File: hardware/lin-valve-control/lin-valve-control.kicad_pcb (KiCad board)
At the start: 4 copper layers, 78.2 x 43.2 mm, 42 parts, among them J1 Screw_Terminal_01x04, J2 Screw_Terminal_01x02, J3 QWIIC Connector, J4 Screw_Terminal_01x03, J5 Screw_Terminal_01x03, J6 DIN5, J7 DIN5, Q1 2N7002, Q2 2N7002, Q3 2N7002, Q4 2N7002, Q5 SUD50P04-08, Q6 SUD50P04-08, U1 Arduino_Nano_v3.x, U2 DRV8833PWP, U3 TJA1021T

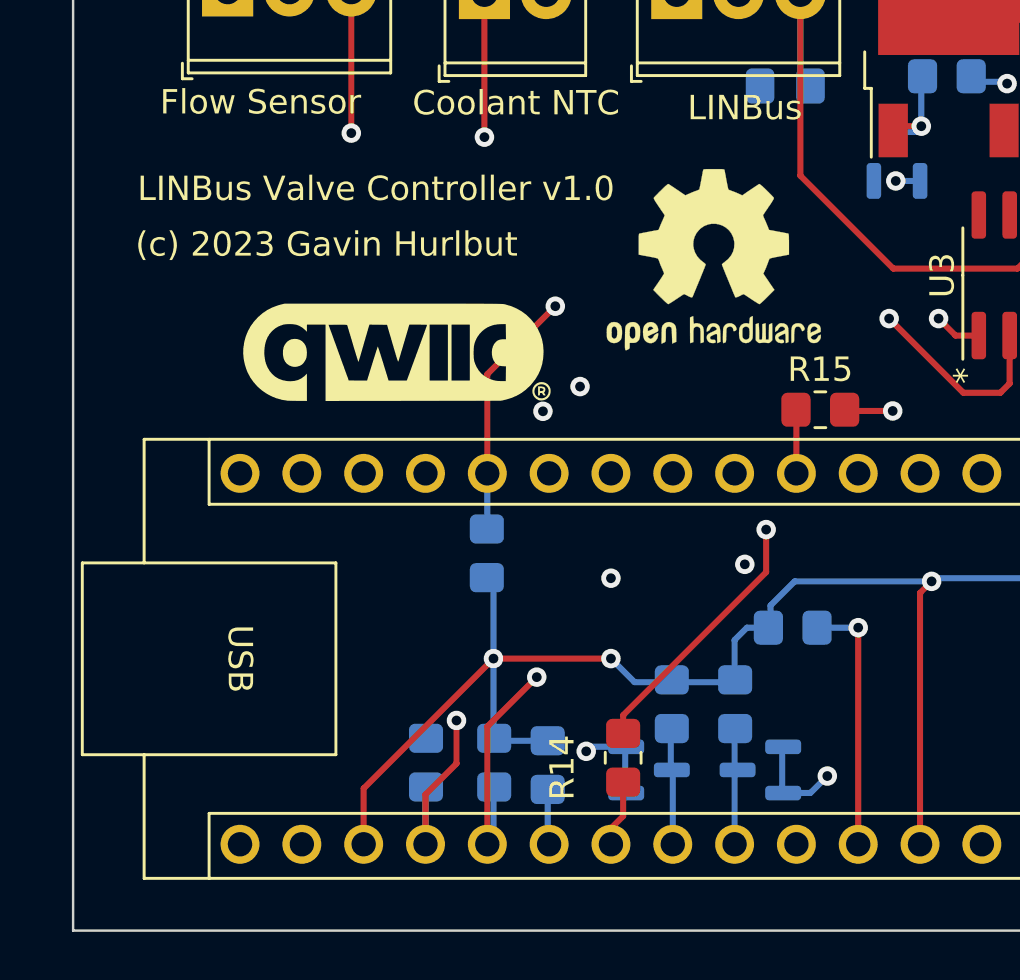
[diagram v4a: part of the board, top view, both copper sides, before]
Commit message: Add a connector to attach 20x4 LCD on an I2C backpack
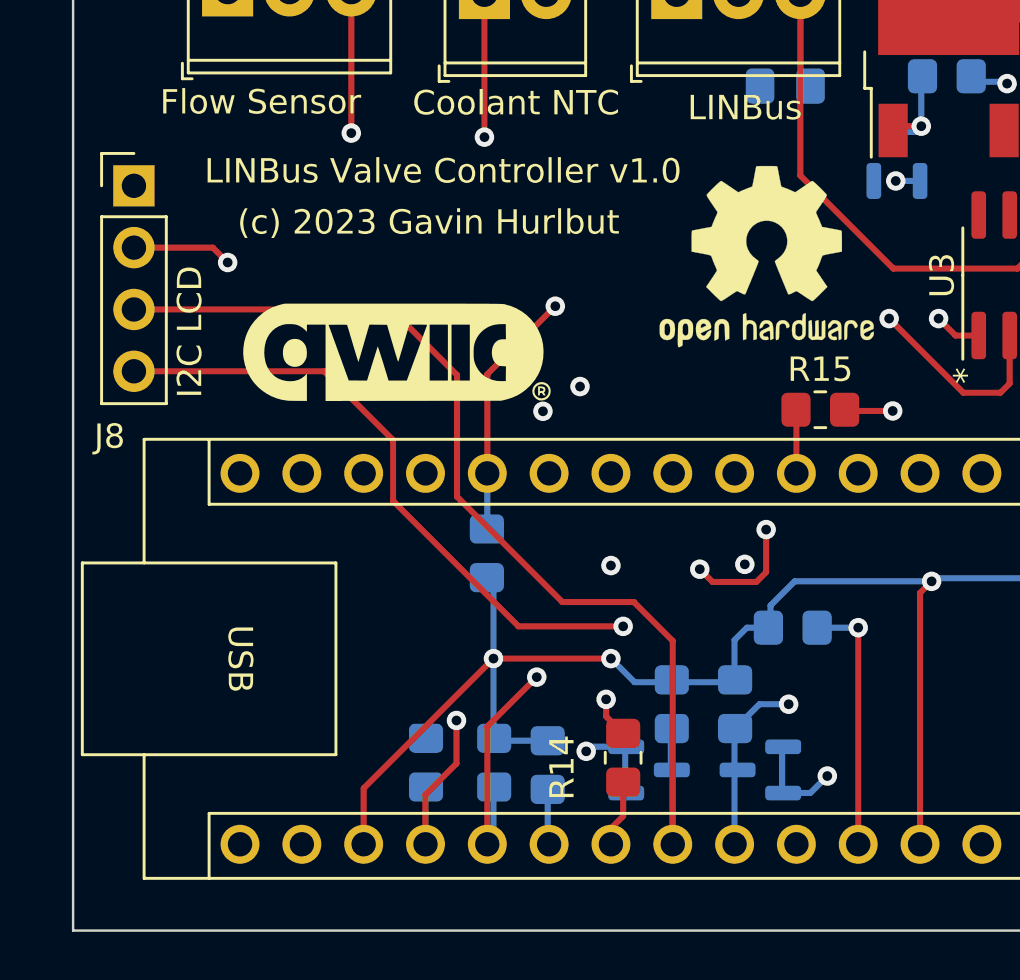
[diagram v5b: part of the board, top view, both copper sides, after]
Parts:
- added J8: I2C LCD, Connector_PinHeader_2.54mm:PinHeader_1x04_P2.54mm_Vertical, F.Cu at (154.9, 71.0)
- moved REF** 2.18 mm to (180.9, 73.9)
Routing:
- net SDA5V: track 4.90 -> 44.0 mm
- net SCL5V: track 4.90 -> 41.5 mm, vias 0 -> 2
- net +5V: track 90.8 -> 95.0 mm, vias 3 -> 4
- net Net-(Q3-Pad1): track 28.3 -> 31.0 mm, vias 2 -> 4
- net VALVE1_CLOSED: track 48.5 -> 50.1 mm
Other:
- board text added: "I2C LCD"

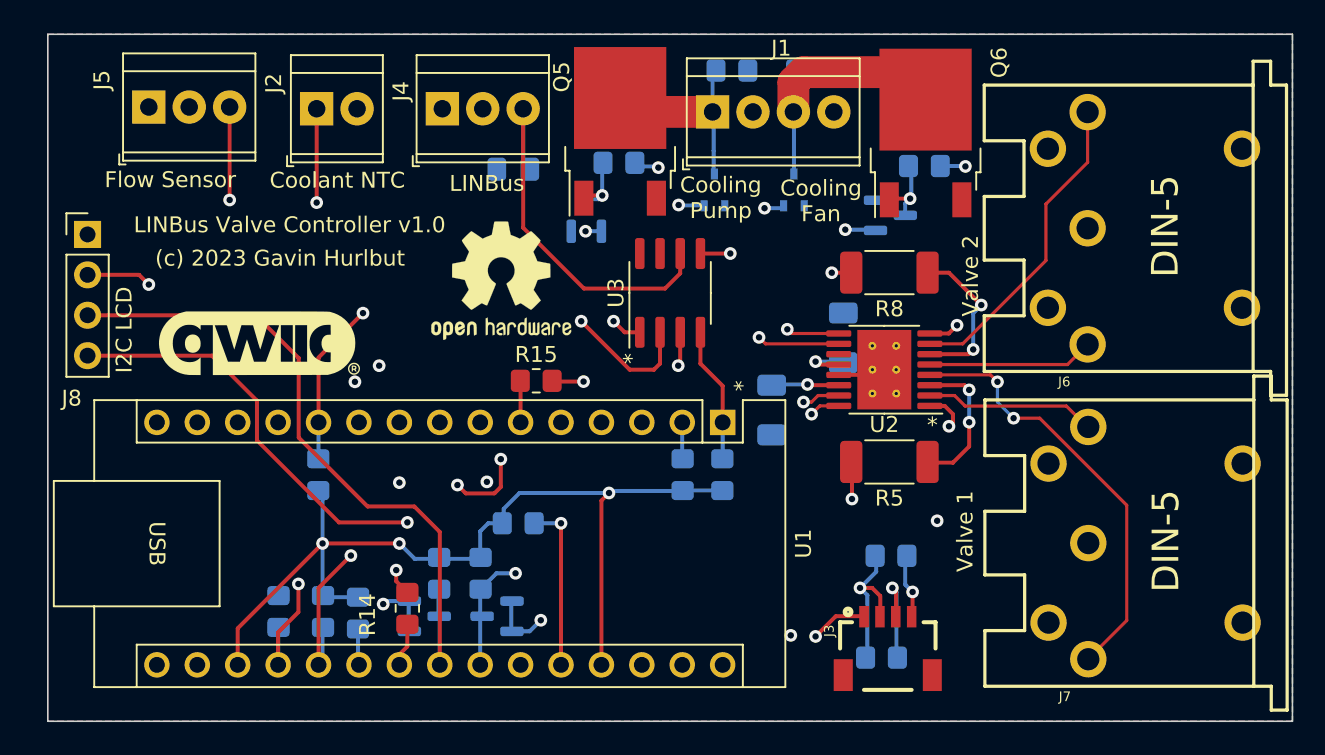
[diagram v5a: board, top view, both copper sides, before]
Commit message: Completely redo the valve controller.  One valve only.
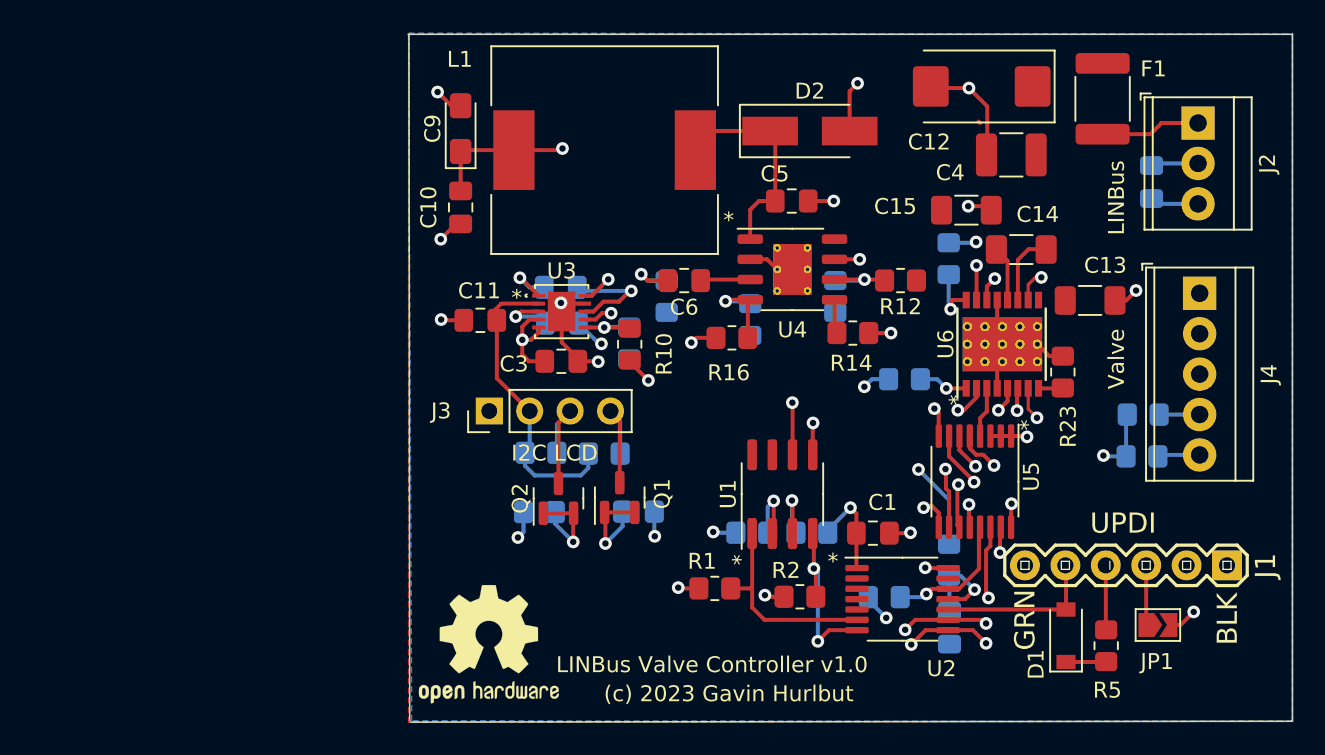
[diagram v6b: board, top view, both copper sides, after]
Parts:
- removed G***: LOGO, Beirdo:qwiic-logo
- removed J5: Screw_Terminal_01x03, TerminalBlock_TE-Connectivity:TerminalBlock_TE_282834-3_1x03_P2.54mm_Horizontal
- removed J6, J7: DIN5, SparkFun-Connectors:DIN5-RA-PTH
- removed J8: I2C LCD, Connector_PinHeader_2.54mm:PinHeader_1x04_P2.54mm_Vertical
- removed Q3, Q4: 2N7002, Package_TO_SOT_SMD:SOT-23
- removed Q5, Q6: SUD50P04-08, Package_TO_SOT_SMD:TO-252-2
- added C10: 10uF, Capacitor_SMD:C_0805_2012Metric_Pad1.18x1.45mm_HandSolder, F.Cu at (178.3, 69.3)
- added C11: 10uF, Capacitor_SMD:C_0805_2012Metric_Pad1.18x1.45mm_HandSolder, F.Cu at (179.6, 76.4)
- added C12: 100uF Ta 25V, Capacitor_Tantalum_SMD:CP_EIA-7343-20_Kemet-V_Pad2.25x2.55mm_HandSolder, F.Cu at (211.1, 61.7)
- added C13: 100nF 25V, Capacitor_SMD:C_1206_3216Metric_Pad1.33x1.80mm_HandSolder, F.Cu at (217.9, 75.2)
- added C14: 100nF 25V, Capacitor_SMD:C_1206_3216Metric_Pad1.33x1.80mm_HandSolder, F.Cu at (213.6, 72.0)
- added C15: 100nF 25V, Capacitor_SMD:C_1206_3216Metric_Pad1.33x1.80mm_HandSolder, F.Cu at (210.1, 69.5)
- added C16: 1nF, Capacitor_SMD:C_0805_2012Metric_Pad1.18x1.45mm_HandSolder, B.Cu at (209.1, 95.7)
- added C4: 10uF 100V, Capacitor_SMD:C_1210_3225Metric_Pad1.33x2.70mm_HandSolder, F.Cu at (213.0, 66.0)
- added C5: 100nF, Capacitor_SMD:C_0805_2012Metric_Pad1.18x1.45mm_HandSolder, F.Cu at (199.2, 68.9)
- added C6: 10nF, Capacitor_SMD:C_0805_2012Metric_Pad1.18x1.45mm_HandSolder, F.Cu at (192.4, 73.9)
- added C7: 2.2uF, Capacitor_SMD:C_0805_2012Metric_Pad1.18x1.45mm_HandSolder, B.Cu at (184.7, 76.6)
- added C8: 2.2uF, Capacitor_SMD:C_0805_2012Metric_Pad1.18x1.45mm_HandSolder, B.Cu at (184.6, 74.3)
- added C9: 100uF Ta 6V, Capacitor_Tantalum_SMD:CP_EIA-3216-10_Kemet-I_Pad1.58x1.35mm_HandSolder, F.Cu at (178.3, 64.3)
- added F1: 3A Polyfuse, Resistor_SMD:R_1812_4532Metric_Pad1.30x3.40mm_HandSolder, F.Cu at (218.7, 62.5)
- added JP1: Solder Jumper, Jumper:SolderJumper-2_P1.3mm_Open_TrianglePad1.0x1.5mm, F.Cu at (222.2, 95.5)
- added L1: 33uH 5A 88mOhm, Beirdo:PM4346.333NLT, F.Cu at (187.4, 65.7)
- added R20: 10k, Resistor_SMD:R_0805_2012Metric_Pad1.20x1.40mm_HandSolder, B.Cu at (221.2, 82.3)
- added R21: 10k, Resistor_SMD:R_0805_2012Metric_Pad1.20x1.40mm_HandSolder, B.Cu at (221.2, 85.0)
- added R22: 10k, Resistor_SMD:R_0805_2012Metric_Pad1.20x1.40mm_HandSolder, B.Cu at (209.1, 91.5)
- added R23: 200m, Resistor_SMD:R_0805_2012Metric_Pad1.20x1.40mm_HandSolder, F.Cu at (216.2, 79.7)
- added R24: 10k, Resistor_SMD:R_0805_2012Metric_Pad1.20x1.40mm_HandSolder, B.Cu at (206.2, 80.1)
- added U4: BD9G341EFJ, Package_SO:HTSOP-8-1EP_3.9x4.9mm_P1.27mm_EP2.4x3.2mm_ThermalVias, F.Cu at (199.2, 73.2)
- added U5: TCA9534, Package_SO:TSSOP-16_4.4x5mm_P0.65mm, F.Cu at (210.7, 86.5)
- added U6: DRV8801PWP, Package_SO:HTSSOP-16-1EP_4.4x5mm_P0.65mm_EP3.4x5mm_Mask3x3mm_ThermalVias, F.Cu at (212.4, 77.9)
- C1: value 10uF 16V -> 100nF; footprint Capacitor_SMD:C_1206_3216Metric_Pad1.33x1.80mm_HandSolder -> Capacitor_SMD:C_0805_2012Metric_Pad1.18x1.45mm_HandSolder; moved to F.Cu
- C3: value 2.2uF 6.3V -> 2.2uF; footprint Capacitor_SMD:C_1206_3216Metric_Pad1.33x1.80mm_HandSolder -> Capacitor_SMD:C_0805_2012Metric_Pad1.18x1.45mm_HandSolder; moved to F.Cu
- D1: value BAT54SW -> BAT42W-V; footprint Package_TO_SOT_SMD:SOT-323_SC-70 -> Diode_SMD:D_SOD-123; moved to F.Cu
- D2: value BAT54SW -> BYS10-35; footprint Package_TO_SOT_SMD:SOT-323_SC-70 -> Diode_SMD:D_SMA_Handsoldering; moved to F.Cu
- J1: value Screw_Terminal_01x04 -> UPDI; footprint TerminalBlock_TE-Connectivity:TerminalBlock_TE_282834-4_1x04_P2.54mm_Horizontal -> Beirdo:FTDI_BASIC
- J2: value Screw_Terminal_01x02 -> Screw_Terminal_01x03; footprint TerminalBlock_TE-Connectivity:TerminalBlock_TE_282834-2_1x02_P2.54mm_Horizontal -> TerminalBlock_TE-Connectivity:TerminalBlock_TE_282834-3_1x03_P2.54mm_Horizontal
- J3: value QWIIC Connector -> I2C LCD; footprint SparkFun-Connectors:1X04_1MM_RA -> Connector_PinHeader_2.54mm:PinHeader_1x04_P2.54mm_Vertical
- J4: value Screw_Terminal_01x03 -> Screw_Terminal_01x05; footprint TerminalBlock_TE-Connectivity:TerminalBlock_TE_282834-3_1x03_P2.54mm_Horizontal -> TerminalBlock_TE-Connectivity:TerminalBlock_TE_282834-5_1x05_P2.54mm_Horizontal
- Q1, Q2, R1, R2: moved to F.Cu
- R10: value 10k -> 357k 1%; moved to F.Cu
- R11: value 10k -> 100k 1%
- R12: value 10k -> 909k 1%; moved to F.Cu
- R13: value 10k -> 324k 1%
- R14: value 10R -> 47k
- R15: value 10R -> 6k2; moved to B.Cu
- R16: value 10k -> 1k3; moved to F.Cu
- R17: value 10k -> 560R
- R18: value 10R -> 100k
- R19: value 10R -> 10k
- R5: value 2R 2W -> 470R; footprint Resistor_SMD:R_2010_5025Metric_Pad1.40x2.65mm_HandSolder -> Resistor_SMD:R_0805_2012Metric_Pad1.20x1.40mm_HandSolder
- R8: value 2R 2W -> 10k; footprint Resistor_SMD:R_2010_5025Metric_Pad1.40x2.65mm_HandSolder -> Resistor_SMD:R_0805_2012Metric_Pad1.20x1.40mm_HandSolder; moved to B.Cu
- U1: value Arduino_Nano_v3.x -> TJA1021T; footprint Module:Arduino_Nano -> Package_SO:SOIC-8_3.9x4.9mm_P1.27mm
- U2: value DRV8833PWP -> ATtiny424-X; footprint Package_SO:HTSSOP-16-1EP_4.4x5mm_P0.65mm_EP3.4x5mm_Mask2.46x2.31mm_ThermalVias -> Package_SO:TSSOP-14_4.4x5mm_P0.65mm
- U3: value TJA1021T -> LTC3203BEDD-PBF; footprint Package_SO:SOIC-8_3.9x4.9mm_P1.27mm -> UltraLibrarian:LTC3203BEDD-PBF
- moved J2 55.4 mm to (224.7, 64.0), turned to -90 degrees
- moved J4 49.0 mm to (224.8, 74.7), turned to -90 degrees
- moved J1 43.1 mm to (226.5, 91.8), turned to 180 degrees
- moved C2 40.1 mm to (221.8, 67.7), turned to 90 degrees
- moved R12 40.0 mm to (206.0, 73.9), turned to 180 degrees
- moved D1 35.7 mm to (216.4, 96.2)
- moved R19 33.4 mm to (205.0, 93.8)
- moved R14 32.9 mm to (203.0, 77.2), turned to 0 degrees
- moved R3 30.2 mm to (196.7, 89.8), turned to 0 degrees
- moved J3 28.2 mm to (180.2, 82.1), turned to 90 degrees
- moved R8 26.7 mm to (183.3, 88.5), turned to 0 degrees
- moved R10 25.6 mm to (189.0, 77.9), turned to 90 degrees
- moved R11 25.3 mm to (188.9, 77.8), turned to 90 degrees
- moved R4 23.6 mm to (200.4, 89.8), turned to 180 degrees
- moved REF** 22.9 mm to (180.1, 96.8)
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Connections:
- C1 pad 1: +12V -> GND
- C1 pad 2: GND -> +3V3
- C3 pad 1: Net-(C3-Pad1) -> +3V3
- D1 pad 1: GND -> Net-(D1-Pad1)
- D1 pad 2: +12V -> UPDI
- D2 pad 1: GND -> Net-(C5-Pad2)
- D2 pad 2: +12V -> GND
- J1 pad 1: COOLANT_PUMP -> GND
- J1 pad 2: GND -> unconnected-(J1-Pad2)
- J1 pad 3: COOLING_FAN -> Net-(J1-Pad3)
- J1 pad 4: GND -> Net-(J1-Pad4)
- J2 pad 1: COOLANT_NTC -> +BATT
- J3 pad 2: +3V3 -> +5V
- J3 pad 3: SDA3V -> SDA5V
- J3 pad 4: SCL3V -> SCL5V
- J4 pad 1: +12V -> VALVE+
- J4 pad 2: GND -> VALVE-
- J4 pad 3: LIN -> GND
- R1 pad 1: +5V -> +3V3
- R1 pad 2: COOLANT_NTC -> RXD
- R10 pad 1: +5V -> +3V3
- R10 pad 2: ~{LIN_WAKE} -> Net-(R10-Pad2)
- R11 pad 1: +3V3 -> GND
- R11 pad 2: SDA3V -> Net-(R10-Pad2)
- R12 pad 1: +5V -> +12V
- R12 pad 2: ~{MOTOR_FAULT} -> Net-(R12-Pad2)
- R13 pad 1: +3V3 -> Net-(R12-Pad2)
- R13 pad 2: SCL3V -> GND
- R14 pad 1: PUMP_EN -> Net-(R14-Pad1)
- R14 pad 2: Net-(Q3-Pad1) -> GND
- R15 pad 1: FAN_PWM -> Net-(C6-Pad2)
- R15 pad 2: Net-(Q4-Pad1) -> GND
- R16 pad 1: +12V -> +3V3
- R16 pad 2: Net-(Q3-Pad3) -> Net-(R16-Pad2)
- R17 pad 1: +12V -> Net-(R16-Pad2)
- R17 pad 2: Net-(Q4-Pad3) -> GND
- R18 pad 1: COOLANT_PUMP -> +3V3
- R18 pad 2: GND -> Net-(R18-Pad2)
- R19 pad 1: COOLING_FAN -> +3V3
- R19 pad 2: GND -> ~{I2C_INT}
- R2 pad 1: +5V -> +3V3
- R2 pad 2: RXD -> TXD
- R3 pad 1: MOTOR_EN -> +3V3
- R3 pad 2: GND -> ~{LIN_SLP}
- R4 pad 1: +5V -> +3V3
- R4 pad 2: SDA5V -> ~{LIN_WAKE}
- R5 pad 1: Net-(R5-Pad1) -> Net-(D1-Pad1)
- R5 pad 2: GND -> Net-(J1-Pad4)
- R6 pad 2: TXD -> SDA5V
- R8 pad 1: Net-(R8-Pad1) -> +3V3
- R8 pad 2: GND -> SDA3V
- R9 pad 1: +5V -> +3V3
- R9 pad 2: ~{LIN_SLP} -> SCL3V
- U1 pad 1: TXD -> RXD
- U1 pad 2: RXD -> ~{LIN_SLP}
- U1 pad 3: unconnected-(U1-Pad3) -> ~{LIN_WAKE}
- U1 pad 4: GND -> TXD
- U1 pad 5: FLOW_PULSE -> GND
- U1 pad 6: FAN_PWM -> LIN
- U1 pad 7: VALVE_IN1+ -> +12V
- U1 pad 8: VALVE_IN1- -> unconnected-(U1-Pad8)
- U2 pad 1: MOTOR_EN -> +3V3
- U2 pad 10: VALVE_IN2- -> UPDI
- U2 pad 11: unconnected-(U2-Pad11) -> VPROPI
- U2 pad 12: +12V -> ~{I2C_INT}
- U2 pad 13: GND -> ~{RESET}
- U2 pad 14: Net-(C3-Pad1) -> GND
- U2 pad 2: VALVE1+ -> unconnected-(U2-Pad2)
- U2 pad 3: Net-(R5-Pad1) -> unconnected-(U2-Pad3)
- U2 pad 4: VALVE1- -> unconnected-(U2-Pad4)
- U2 pad 5: VALVE2- -> unconnected-(U2-Pad5)
- U2 pad 6: Net-(R8-Pad1) -> RXD
- U2 pad 7: VALVE2+ -> TXD
- U2 pad 8: ~{MOTOR_FAULT} -> SDA3V
- U2 pad 9: VALVE_IN2+ -> SCL3V
- U3 pad 1: RXD -> Net-(C8-Pad1)
- U3 pad 2: ~{LIN_SLP} -> +5V
- U3 pad 3: ~{LIN_WAKE} -> Net-(C7-Pad2)
- U3 pad 4: TXD -> +3V3
- U3 pad 5: GND -> +3V3
- U3 pad 6: LIN -> Net-(R10-Pad2)
- U3 pad 7: +12V -> +3V3
- U3 pad 8: unconnected-(U3-Pad8) -> Net-(C8-Pad2)
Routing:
- net +5V: track 95.0 -> 18.9 mm, vias 4 -> 0
- net VALVE2_OPEN: track 63.1 -> 0.00 mm
- net ~{MOTOR_FAULT}: track 59.9 -> 0.00 mm, vias 3 -> 0
- net VALVE2_CLOSED: track 57.4 -> 0.00 mm
- net MOTOR_EN: track 56.0 -> 0.00 mm, vias 2 -> 0
- net VALVE1_CLOSED: track 50.1 -> 0.00 mm, vias 1 -> 0
- net VALVE1_OPEN: track 48.1 -> 0.00 mm
- net COOLANT_NTC: track 44.9 -> 0.00 mm, vias 2 -> 0
- net VALVE_IN2-: track 40.2 -> 0.00 mm, vias 1 -> 0
- net VALVE_IN2+: track 37.8 -> 0.00 mm, vias 1 -> 0
- net SDA5V: track 44.0 -> 7.82 mm
- net FLOW_PULSE: track 34.8 -> 0.00 mm, vias 2 -> 0
- net SCL5V: track 41.5 -> 7.67 mm, vias 2 -> 0
- net GND: track 11.6 -> 44.7 mm, vias 4 -> 14
- net Net-(Q3-Pad1): track 31.0 -> 0.00 mm, vias 4 -> 0
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- added copper zone on In2.Cu, net +3V3
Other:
- board size 78.2 x 43.2 mm -> 55.6 x 43.2 mm
- board text added: "Valve"
- board text removed: "Coolant NTC"
- board text removed: "Cooling Fan"
- board text removed: "Cooling Pump"
- board text removed: "Flow Sensor"
- board text removed: "Valve 1"
- board text removed: "Valve 2"

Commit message: Add PCA9536 for the LINBus Address
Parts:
- added JP2: A3, Jumper:SolderJumper-2_P1.3mm_Open_TrianglePad1.0x1.5mm, B.Cu at (194.1, 97.0)
- added JP3: A2, Jumper:SolderJumper-2_P1.3mm_Open_TrianglePad1.0x1.5mm, B.Cu at (191.4, 97.0)
- added JP4: A1, Jumper:SolderJumper-2_P1.3mm_Open_TrianglePad1.0x1.5mm, B.Cu at (188.8, 97.1)
- added JP5: A0, Jumper:SolderJumper-2_P1.3mm_Open_TrianglePad1.0x1.5mm, B.Cu at (186.3, 97.2)
- added U3: PCA9536DP, Package_SO:TSSOP-8_3x3mm_P0.65mm, F.Cu at (187.9, 93.2)
- renumbered J3 to J2, J2 to J3, U3 to U4, U4 to U5, U5 to U6, U6 to U7
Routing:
- net Net-(JP5-Pad2): track 0.00 -> 9.66 mm, vias 0 -> 2
- net Net-(JP4-Pad2): track 0.00 -> 8.13 mm, vias 0 -> 1
- net Net-(JP3-Pad2): track 0.00 -> 7.65 mm, vias 0 -> 1
- net Net-(JP2-Pad2): track 0.00 -> 5.65 mm, vias 0 -> 1
- net SDA3V: track 44.7 -> 47.7 mm, vias 4 -> 5
- net GND: track 44.7 -> 47.5 mm, vias 14 -> 15
- net SCL3V: track 39.7 -> 41.5 mm, vias 4 -> 5
- net +3V3: track 46.4 -> 47.7 mm, vias 17 -> 18

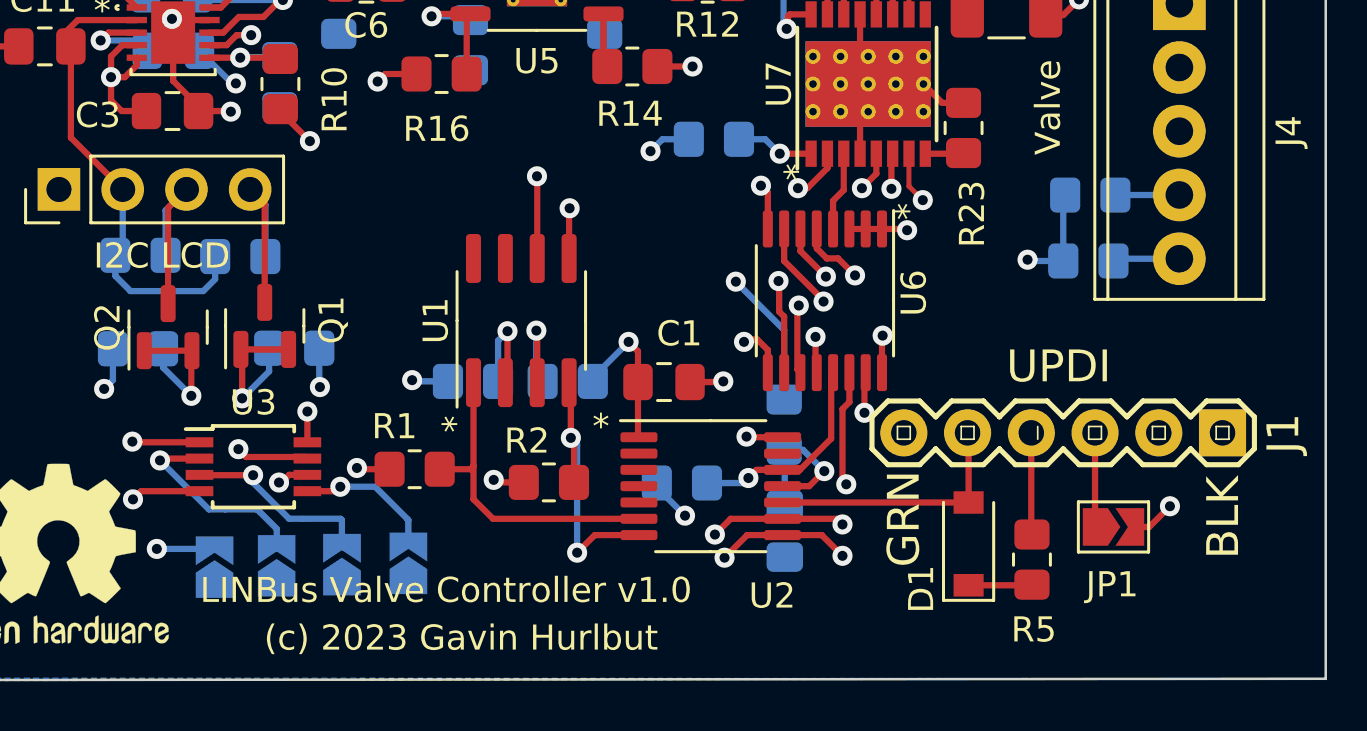
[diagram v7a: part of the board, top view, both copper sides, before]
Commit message: Get this in place (barely) on ATTiny824.
- should not be THAT big, I thought.  Investigation to follow:

Sketch uses 7998 bytes (97%) of program storage space. Maximum is 8192 bytes.
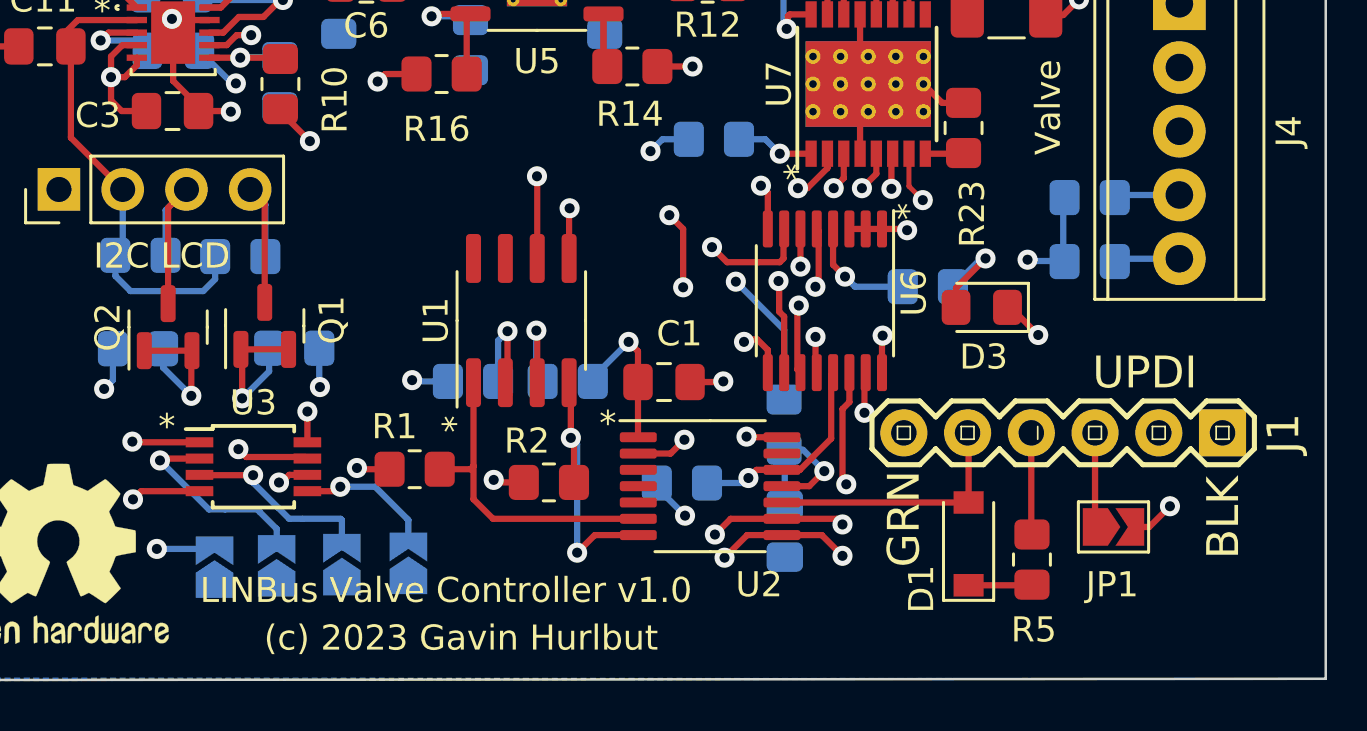
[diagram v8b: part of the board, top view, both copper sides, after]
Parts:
- added D3: LED, LED_SMD:LED_0805_2012Metric_Pad1.15x1.40mm_HandSolder, F.Cu at (216.9, 86.8)
- added R25: 330, Resistor_SMD:R_0805_2012Metric_Pad1.20x1.40mm_HandSolder, B.Cu at (214.8, 86.0)
- U2: value ATtiny424-X -> ATtiny824-X
- moved R20 2.65 mm to (221.2, 85.0)
- moved R21 2.53 mm to (221.2, 82.4)
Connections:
- R20 pad 2: ~{VALVE_OPEN} -> ~{VALVE_CLOSED}
- R21 pad 2: ~{VALVE_CLOSED} -> ~{VALVE_OPEN}
- U2 pad 2: unconnected-(U2-Pad2) -> PHASE
- U6 pad 4: PHASE -> Net-(U6-Pad4)
- U6 pad 7: ~{VALVE_OPEN} -> ~{VALVE_CLOSED}
- U6 pad 9: ~{VALVE_CLOSED} -> ~{VALVE_OPEN}
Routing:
- net PHASE: track 3.18 -> 19.8 mm, vias 0 -> 4
- net Net-(U6-Pad4): track 0.00 -> 4.56 mm, vias 0 -> 1
- net Net-(D3-Pad2): track 0.00 -> 4.20 mm, vias 0 -> 1
- net ~{VALVE_OPEN}: track 22.0 -> 24.9 mm
- net GND: track 47.5 -> 49.2 mm, vias 15 -> 16
- net ~{SLEEP}: track 8.05 -> 7.25 mm
- net ENABLE: track 8.22 -> 8.96 mm
